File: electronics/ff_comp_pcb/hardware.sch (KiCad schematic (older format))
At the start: 32 parts, among them U2 A33

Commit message: Dropped down the board to board.
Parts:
- added J3: Conn_01x08_Female, Connector_PinHeader_2.54mm:PinHeader_1x08_P2.54mm_Vertical, symbol Connector:Conn_01x08_Female
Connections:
- net labels added: +5V
- wire segments 350 -> 368
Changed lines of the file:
@@
 $EndSheet
 $Sheet
-S 4800 6000 1450 1100
+S 3600 6500 1450 1100
 U 6063BE69
 F0 "gpio" 50
@@
 Connection ~ 5200 1700
 Connection ~ 8500 2800
+$Comp
+L power:+1V1 #PWR?
+U 1 1 60EAFA58
+P 5150 5550
+AR Path="/60A30BFF/60EAFA58" Ref="#PWR?"  Part="1"
+AR Path="/60EAFA58" Ref="#PWR022"  Part="1"
+F 0 "#PWR022" H 5150 5400 50  0001 C CNN
+F 1 "+1V1" H 5165 5723 50  0000 C CNN
+F 2 "" H 5150 5550 50  0001 C CNN
+F 3 "" H 5150 5550 50  0001 C CNN
+	1    5150 5550
+	1    0    0    -1
+$EndComp
+$Comp
+L power:+3V3 #PWR?
+U 1 1 60EB04B1
+P 6150 5550
+AR Path="/60A30BFF/60EB04B1" Ref="#PWR?"  Part="1"
+AR Path="/60EB04B1" Ref="#PWR026"  Part="1"
+F 0 "#PWR026" H 6150 5400 50  0001 C CNN
+F 1 "+3V3" H 6165 5723 50  0000 C CNN
+F 2 "" H 6150 5550 50  0001 C CNN
+F 3 "" H 6150 5550 50  0001 C CNN
+	1    6150 5550
+	1    0    0    -1
+$EndComp
+$Comp
+L power:+2V5 #PWR?
+U 1 1 60EB102A
+P 5700 5550
+AR Path="/60A30BFF/60EB102A" Ref="#PWR?"  Part="1"
+AR Path="/60EB102A" Ref="#PWR024"  Part="1"
+F 0 "#PWR024" H 5700 5400 50  0001 C CNN
+F 1 "+2V5" H 5715 5723 50  0000 C CNN
+F 2 "" H 5700 5550 50  0001 C CNN
+F 3 "" H 5700 5550 50  0001 C CNN
+	1    5700 5550
+	1    0    0    -1
+$EndComp
+$Comp
+L power:+3V0 #PWR?
+U 1 1 60EB5386
+P 5950 5550
+AR Path="/60A30BFF/60EB5386" Ref="#PWR?"  Part="1"
+AR Path="/60EB5386" Ref="#PWR025"  Part="1"
+F 0 "#PWR025" H 5950 5400 50  0001 C CNN
+F 1 "+3V0" H 5965 5723 50  0000 C CNN
+F 2 "" H 5950 5550 50  0001 C CNN
+F 3 "" H 5950 5550 50  0001 C CNN
+	1    5950 5550
+	1    0    0    -1
+$EndComp
+$Comp
+L power:+1V35 #PWR?
+U 1 1 60EB6725
+P 5400 5550
+AR Path="/60536DA4/60EB6725" Ref="#PWR?"  Part="1"
+AR Path="/60A30BFF/60EB6725" Ref="#PWR?"  Part="1"
+AR Path="/60EB6725" Ref="#PWR023"  Part="1"
+F 0 "#PWR023" H 5400 5400 50  0001 C CNN
+F 1 "+1V35" H 5415 5723 50  0000 C CNN
+F 2 "" H 5400 5550 50  0001 C CNN
+F 3 "" H 5400 5550 50  0001 C CNN
+	1    5400 5550
+	1    0    0    -1
+$EndComp
+$Comp
+L power:+5V #PWR027
+U 1 1 60EE46D3
+P 6350 5550
+F 0 "#PWR027" H 6350 5400 50  0001 C CNN
+F 1 "+5V" H 6365 5723 50  0000 C CNN
+F 2 "" H 6350 5550 50  0001 C CNN
+F 3 "" H 6350 5550 50  0001 C CNN
+	1    6350 5550
+	1    0    0    -1
+$EndComp
+Wire Wire Line
+	6350 5550 6350 5700
+Wire Wire Line
+	6350 5700 6500 5700
+Wire Wire Line
+	6150 5550 6150 5800
+Wire Wire Line
+	6150 5800 6500 5800
+Wire Wire Line
+	5950 5550 5950 5900
+Wire Wire Line
+	5950 5900 6500 5900
+Wire Wire Line
+	5700 5550 5700 6000
+Wire Wire Line
+	5400 5550 5400 6100
+Wire Wire Line
+	5400 6100 6500 6100
+Wire Wire Line
+	6500 6200 5150 6200
+Wire Wire Line
+	6500 6300 6400 6300
+Wire Wire Line
+	6400 6300 6400 6450
+$Comp
+L power:GND #PWR?
+U 1 1 611BFAF5
+P 6400 6450
+AR Path="/60536DA4/611BFAF5" Ref="#PWR?"  Part="1"
+AR Path="/611BFAF5" Ref="#PWR028"  Part="1"
+AR Path="/60A30BFF/611BFAF5" Ref="#PWR?"  Part="1"
+F 0 "#PWR028" H 6400 6200 50  0001 C CNN
+F 1 "GND" V 6405 6322 50  0001 R CNN
+F 2 "" H 6400 6450 50  0001 C CNN
+F 3 "" H 6400 6450 50  0001 C CNN
+	1    6400 6450
+	1    0    0    -1
+$EndComp
+$Comp
+L Connector:Conn_01x08_Female J3
+U 1 1 611D7C88
+P 6700 5900
+F 0 "J3" H 6728 5830 50  0000 L CNN
+F 1 "Conn_01x08_Female" H 6728 5785 50  0001 L CNN
+F 2 "Connector_PinHeader_2.54mm:PinHeader_1x08_P2.54mm_Vertical" H 6700 5900 50  0001 C CNN
+F 3 "~" H 6700 5900 50  0001 C CNN
+	1    6700 5900
+	1    0    0    -1
+$EndComp
+Wire Wire Line
+	6500 6000 5700 6000
+Wire Wire Line
+	5150 6200 5150 5550
+$Comp
+L power:GND #PWR?
+U 1 1 613D9A97
+P 6900 5550
+AR Path="/60536DA4/613D9A97" Ref="#PWR?"  Part="1"
+AR Path="/613D9A97" Ref="#PWR029"  Part="1"
+AR Path="/60A30BFF/613D9A97" Ref="#PWR?"  Part="1"
+F 0 "#PWR029" H 6900 5300 50  0001 C CNN
+F 1 "GND" V 6905 5422 50  0001 R CNN
+F 2 "" H 6900 5550 50  0001 C CNN
+F 3 "" H 6900 5550 50  0001 C CNN
+	1    6900 5550
+	1    0    0    -1
+$EndComp
+Wire Wire Line
+	6500 5600 6450 5600
+Wire Wire Line
+	6450 5600 6450 5450
+Wire Wire Line
+	6450 5450 6900 5450
+Wire Wire Line
+	6900 5450 6900 5550
 Wire Bus Line
 	3950 3400 3950 3600

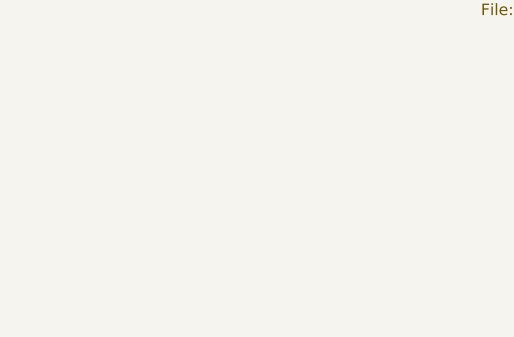
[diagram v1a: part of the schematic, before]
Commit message: Put a mounting hole in the board.
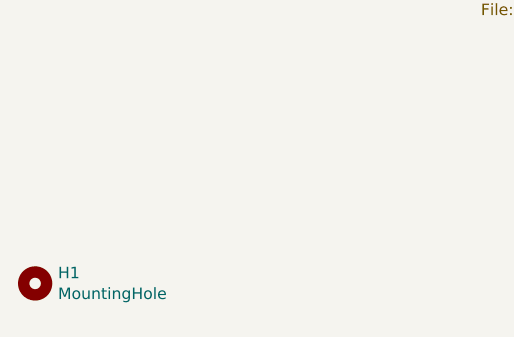
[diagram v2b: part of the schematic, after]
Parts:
- added H1: MountingHole, MountingHole:MountingHole_3.2mm_M3, symbol Mechanical:MountingHole
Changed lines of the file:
@@
 Wire Wire Line
 	6900 5450 6900 5550
+$Comp
+L Mechanical:MountingHole H1
+U 1 1 61489B61
+P 700 7550
+F 0 "H1" H 800 7596 50  0000 L CNN
+F 1 "MountingHole" H 800 7505 50  0000 L CNN
+F 2 "MountingHole:MountingHole_3.2mm_M3" H 700 7550 50  0001 C CNN
+F 3 "~" H 700 7550 50  0001 C CNN
+	1    700  7550
+	1    0    0    -1
+$EndComp
 Wire Bus Line
 	3950 3400 3950 3600

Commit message: Finished up the routing on the power board, still needs a double check.
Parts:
- removed J3: Conn_01x08_Female, Connector_PinHeader_2.54mm:PinHeader_1x08_P2.54mm_Vertical, symbol Connector:Conn_01x08_Female
- added J3: Conn_01x07_Female, Connector_PinHeader_2.54mm:PinHeader_1x07_P2.54mm_Vertical, symbol Connector:Conn_01x07_Female
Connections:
- wire segments 368 -> 366
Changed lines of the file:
@@
 	6500 6200 5150 6200
-Wire Wire Line
-	6500 6300 6400 6300
-Wire Wire Line
-	6400 6300 6400 6450
-$Comp
-L power:GND #PWR?
-U 1 1 611BFAF5
-P 6400 6450
-AR Path="/60536DA4/611BFAF5" Ref="#PWR?"  Part="1"
-AR Path="/611BFAF5" Ref="#PWR028"  Part="1"
-AR Path="/60A30BFF/611BFAF5" Ref="#PWR?"  Part="1"
-F 0 "#PWR028" H 6400 6200 50  0001 C CNN
-F 1 "GND" V 6405 6322 50  0001 R CNN
-F 2 "" H 6400 6450 50  0001 C CNN
-F 3 "" H 6400 6450 50  0001 C CNN
-	1    6400 6450
-	1    0    0    -1
-$EndComp
-$Comp
-L Connector:Conn_01x08_Female J3
-U 1 1 611D7C88
-P 6700 5900
-F 0 "J3" H 6728 5830 50  0000 L CNN
-F 1 "Conn_01x08_Female" H 6728 5785 50  0001 L CNN
-F 2 "Connector_PinHeader_2.54mm:PinHeader_1x08_P2.54mm_Vertical" H 6700 5900 50  0001 C CNN
-F 3 "~" H 6700 5900 50  0001 C CNN
-	1    6700 5900
-	1    0    0    -1
-$EndComp
 Wire Wire Line
 	6500 6000 5700 6000
@@
 Wire Bus Line
 	4050 1700 4050 3300
+$Comp
+L Connector:Conn_01x07_Female J3
+U 1 1 6110DED7
+P 6700 5900
+F 0 "J3" H 6728 5926 50  0000 L CNN
+F 1 "Conn_01x07_Female" H 6728 5835 50  0000 L CNN
+F 2 "Connector_PinHeader_2.54mm:PinHeader_1x07_P2.54mm_Vertical" H 6700 5900 50  0001 C CNN
+F 3 "~" H 6700 5900 50  0001 C CNN
+	1    6700 5900
+	1    0    0    -1
+$EndComp
 $EndSCHEMATC

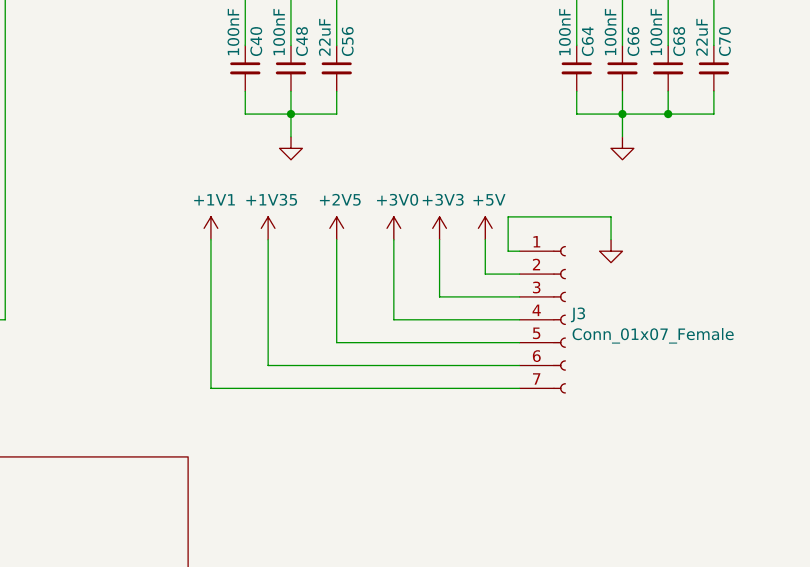
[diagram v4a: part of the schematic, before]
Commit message: Power distrobution IP on the CPU board. Transistors in for 5V control. Part numbers in.
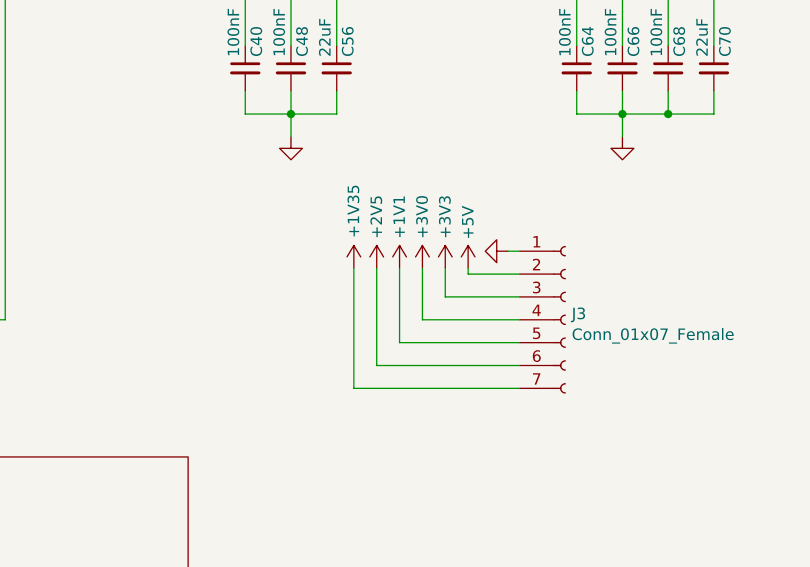
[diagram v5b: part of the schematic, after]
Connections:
- net +1V1: now also J3.5 (Pin_5); no longer J3.7 (Pin_7)
- net +1V35: now also J3.7 (Pin_7); no longer J3.6 (Pin_6)
- net +2V5: now also J3.6 (Pin_6); no longer J3.5 (Pin_5)
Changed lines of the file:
@@
 L power:+1V1 #PWR?
 U 1 1 60EAFA58
-P 5150 5550
+P 5975 5675
 AR Path="/60A30BFF/60EAFA58" Ref="#PWR?"  Part="1"
 AR Path="/60EAFA58" Ref="#PWR022"  Part="1"
-F 0 "#PWR022" H 5150 5400 50  0001 C CNN
-F 1 "+1V1" H 5165 5723 50  0000 C CNN
-F 2 "" H 5150 5550 50  0001 C CNN
-F 3 "" H 5150 5550 50  0001 C CNN
-	1    5150 5550
-	1    0    0    -1
-$EndComp
-$Comp
-L power:+3V3 #PWR?
-U 1 1 60EB04B1
-P 6150 5550
-AR Path="/60A30BFF/60EB04B1" Ref="#PWR?"  Part="1"
-AR Path="/60EB04B1" Ref="#PWR026"  Part="1"
-F 0 "#PWR026" H 6150 5400 50  0001 C CNN
-F 1 "+3V3" H 6165 5723 50  0000 C CNN
-F 2 "" H 6150 5550 50  0001 C CNN
-F 3 "" H 6150 5550 50  0001 C CNN
-	1    6150 5550
+F 0 "#PWR022" H 5975 5525 50  0001 C CNN
+F 1 "+1V1" V 5975 5900 50  0000 C CNN
+F 2 "" H 5975 5675 50  0001 C CNN
+F 3 "" H 5975 5675 50  0001 C CNN
+	1    5975 5675
 	1    0    0    -1
 $EndComp
@@
 L power:+2V5 #PWR?
 U 1 1 60EB102A
-P 5700 5550
+P 5875 5675
 AR Path="/60A30BFF/60EB102A" Ref="#PWR?"  Part="1"
 AR Path="/60EB102A" Ref="#PWR024"  Part="1"
-F 0 "#PWR024" H 5700 5400 50  0001 C CNN
-F 1 "+2V5" H 5715 5723 50  0000 C CNN
-F 2 "" H 5700 5550 50  0001 C CNN
-F 3 "" H 5700 5550 50  0001 C CNN
-	1    5700 5550
-	1    0    0    -1
-$EndComp
-$Comp
-L power:+3V0 #PWR?
-U 1 1 60EB5386
-P 5950 5550
-AR Path="/60A30BFF/60EB5386" Ref="#PWR?"  Part="1"
-AR Path="/60EB5386" Ref="#PWR025"  Part="1"
-F 0 "#PWR025" H 5950 5400 50  0001 C CNN
-F 1 "+3V0" H 5965 5723 50  0000 C CNN
-F 2 "" H 5950 5550 50  0001 C CNN
-F 3 "" H 5950 5550 50  0001 C CNN
-	1    5950 5550
+F 0 "#PWR024" H 5875 5525 50  0001 C CNN
+F 1 "+2V5" V 5875 5900 50  0000 C CNN
+F 2 "" H 5875 5675 50  0001 C CNN
+F 3 "" H 5875 5675 50  0001 C CNN
+	1    5875 5675
 	1    0    0    -1
 $EndComp
@@
 L power:+1V35 #PWR?
 U 1 1 60EB6725
-P 5400 5550
+P 5775 5675
 AR Path="/60536DA4/60EB6725" Ref="#PWR?"  Part="1"
 AR Path="/60A30BFF/60EB6725" Ref="#PWR?"  Part="1"
 AR Path="/60EB6725" Ref="#PWR023"  Part="1"
-F 0 "#PWR023" H 5400 5400 50  0001 C CNN
-F 1 "+1V35" H 5415 5723 50  0000 C CNN
-F 2 "" H 5400 5550 50  0001 C CNN
-F 3 "" H 5400 5550 50  0001 C CNN
-	1    5400 5550
-	1    0    0    -1
-$EndComp
-$Comp
-L power:+5V #PWR027
-U 1 1 60EE46D3
-P 6350 5550
-F 0 "#PWR027" H 6350 5400 50  0001 C CNN
-F 1 "+5V" H 6365 5723 50  0000 C CNN
-F 2 "" H 6350 5550 50  0001 C CNN
-F 3 "" H 6350 5550 50  0001 C CNN
-	1    6350 5550
+F 0 "#PWR023" H 5775 5525 50  0001 C CNN
+F 1 "+1V35" V 5775 5925 50  0000 C CNN
+F 2 "" H 5775 5675 50  0001 C CNN
+F 3 "" H 5775 5675 50  0001 C CNN
+	1    5775 5675
 	1    0    0    -1
 $EndComp
 Wire Wire Line
-	6350 5550 6350 5700
+	6075 5900 6500 5900
 Wire Wire Line
-	6350 5700 6500 5700
+	5975 5675 5975 6000
 Wire Wire Line
-	6150 5550 6150 5800
+	5875 5675 5875 6100
 Wire Wire Line
-	6150 5800 6500 5800
+	5875 6100 6500 6100
 Wire Wire Line
-	5950 5550 5950 5900
+	6500 6200 5775 6200
 Wire Wire Line
-	5950 5900 6500 5900
+	6500 6000 5975 6000
 Wire Wire Line
-	5700 5550 5700 6000
-Wire Wire Line
-	5400 5550 5400 6100
-Wire Wire Line
-	5400 6100 6500 6100
-Wire Wire Line
-	6500 6200 5150 6200
-Wire Wire Line
-	6500 6000 5700 6000
-Wire Wire Line
-	5150 6200 5150 5550
-$Comp
-L power:GND #PWR?
-U 1 1 613D9A97
-P 6900 5550
-AR Path="/60536DA4/613D9A97" Ref="#PWR?"  Part="1"
-AR Path="/613D9A97" Ref="#PWR029"  Part="1"
-AR Path="/60A30BFF/613D9A97" Ref="#PWR?"  Part="1"
-F 0 "#PWR029" H 6900 5300 50  0001 C CNN
-F 1 "GND" V 6905 5422 50  0001 R CNN
-F 2 "" H 6900 5550 50  0001 C CNN
-F 3 "" H 6900 5550 50  0001 C CNN
-	1    6900 5550
-	1    0    0    -1
-$EndComp
+	5775 6200 5775 5675
 Wire Wire Line
 	6500 5600 6450 5600
-Wire Wire Line
-	6450 5600 6450 5450
-Wire Wire Line
-	6450 5450 6900 5450
-Wire Wire Line
-	6900 5450 6900 5550
 $Comp
 L Mechanical:MountingHole H1
@@
 	1    0    0    -1
 $EndComp
+Wire Wire Line
+	6175 5800 6500 5800
+Wire Wire Line
+	6175 5675 6175 5800
+$Comp
+L power:+3V3 #PWR?
+U 1 1 60EB04B1
+P 6175 5675
+AR Path="/60A30BFF/60EB04B1" Ref="#PWR?"  Part="1"
+AR Path="/60EB04B1" Ref="#PWR026"  Part="1"
+F 0 "#PWR026" H 6175 5525 50  0001 C CNN
+F 1 "+3V3" V 6175 5900 50  0000 C CNN
+F 2 "" H 6175 5675 50  0001 C CNN
+F 3 "" H 6175 5675 50  0001 C CNN
+	1    6175 5675
+	1    0    0    -1
+$EndComp
+Wire Wire Line
+	6275 5700 6500 5700
+Wire Wire Line
+	6275 5675 6275 5700
+$Comp
+L power:+5V #PWR027
+U 1 1 60EE46D3
+P 6275 5675
+F 0 "#PWR027" H 6275 5525 50  0001 C CNN
+F 1 "+5V" V 6275 5875 50  0000 C CNN
+F 2 "" H 6275 5675 50  0001 C CNN
+F 3 "" H 6275 5675 50  0001 C CNN
+	1    6275 5675
+	1    0    0    -1
+$EndComp
+Wire Wire Line
+	6075 5675 6075 5900
+$Comp
+L power:+3V0 #PWR?
+U 1 1 60EB5386
+P 6075 5675
+AR Path="/60A30BFF/60EB5386" Ref="#PWR?"  Part="1"
+AR Path="/60EB5386" Ref="#PWR025"  Part="1"
+F 0 "#PWR025" H 6075 5525 50  0001 C CNN
+F 1 "+3V0" V 6075 5900 50  0000 C CNN
+F 2 "" H 6075 5675 50  0001 C CNN
+F 3 "" H 6075 5675 50  0001 C CNN
+	1    6075 5675
+	1    0    0    -1
+$EndComp
+$Comp
+L power:GND #PWR?
+U 1 1 613D9A97
+P 6450 5600
+AR Path="/60536DA4/613D9A97" Ref="#PWR?"  Part="1"
+AR Path="/613D9A97" Ref="#PWR029"  Part="1"
+AR Path="/60A30BFF/613D9A97" Ref="#PWR?"  Part="1"
+F 0 "#PWR029" H 6450 5350 50  0001 C CNN
+F 1 "GND" V 6455 5472 50  0001 R CNN
+F 2 "" H 6450 5600 50  0001 C CNN
+F 3 "" H 6450 5600 50  0001 C CNN
+	1    6450 5600
+	0    1    1    0
+$EndComp
 Wire Bus Line

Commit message: Added gerbers for R0.1 comp pcb.
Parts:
- removed H1: MountingHole, MountingHole:MountingHole_3.2mm_M3, symbol Mechanical:MountingHole
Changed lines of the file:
@@
 	6500 5600 6450 5600
-$Comp
-L Mechanical:MountingHole H1
-U 1 1 61489B61
-P 700 7550
-F 0 "H1" H 800 7596 50  0000 L CNN
-F 1 "MountingHole" H 800 7505 50  0000 L CNN
-F 2 "MountingHole:MountingHole_3.2mm_M3" H 700 7550 50  0001 C CNN
-F 3 "~" H 700 7550 50  0001 C CNN
-	1    700  7550
-	1    0    0    -1
-$EndComp
 $Comp
 L Connector:Conn_01x07_Female J3
